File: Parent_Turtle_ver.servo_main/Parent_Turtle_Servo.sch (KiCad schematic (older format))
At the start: 42 parts, among them P1 CONN_02X15, P10 WRITING, P12 5V_in, P2 CONN_02X15, P3 CAN, P4 CAN, P5 PWM, P6 SERIAL0, P7 SERIAL1, P8 WRITING_IN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

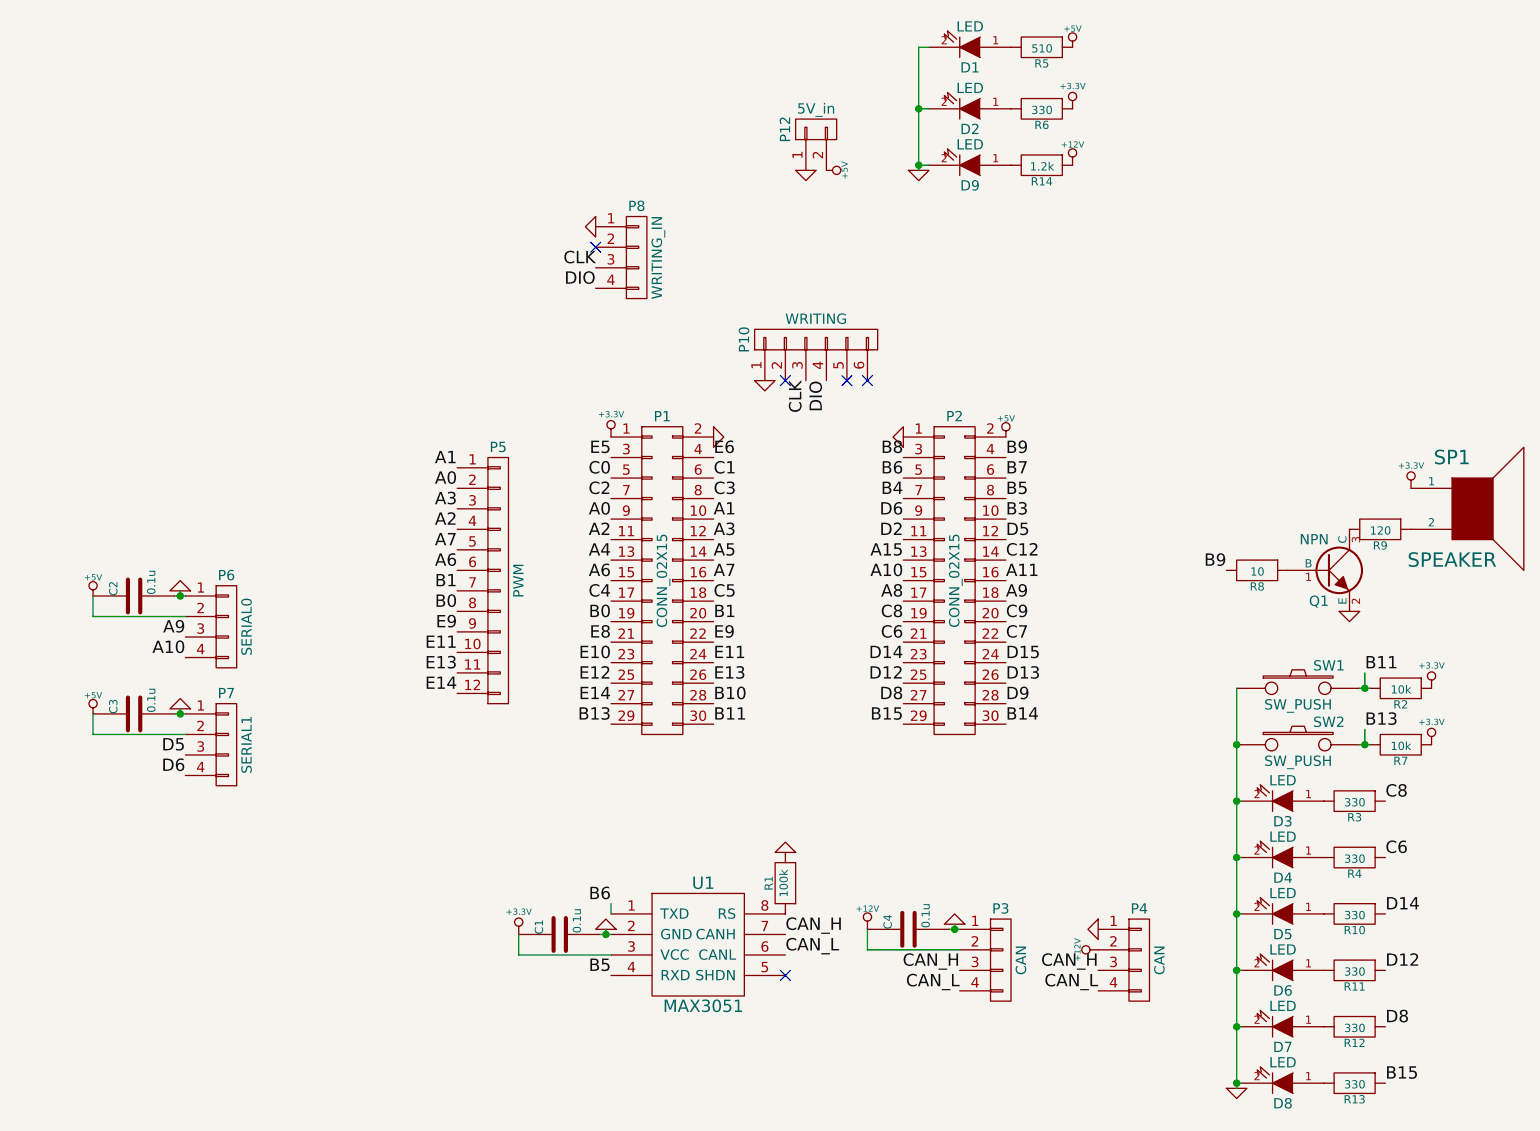
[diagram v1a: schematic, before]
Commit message: A/Dコンバータのピンの追加
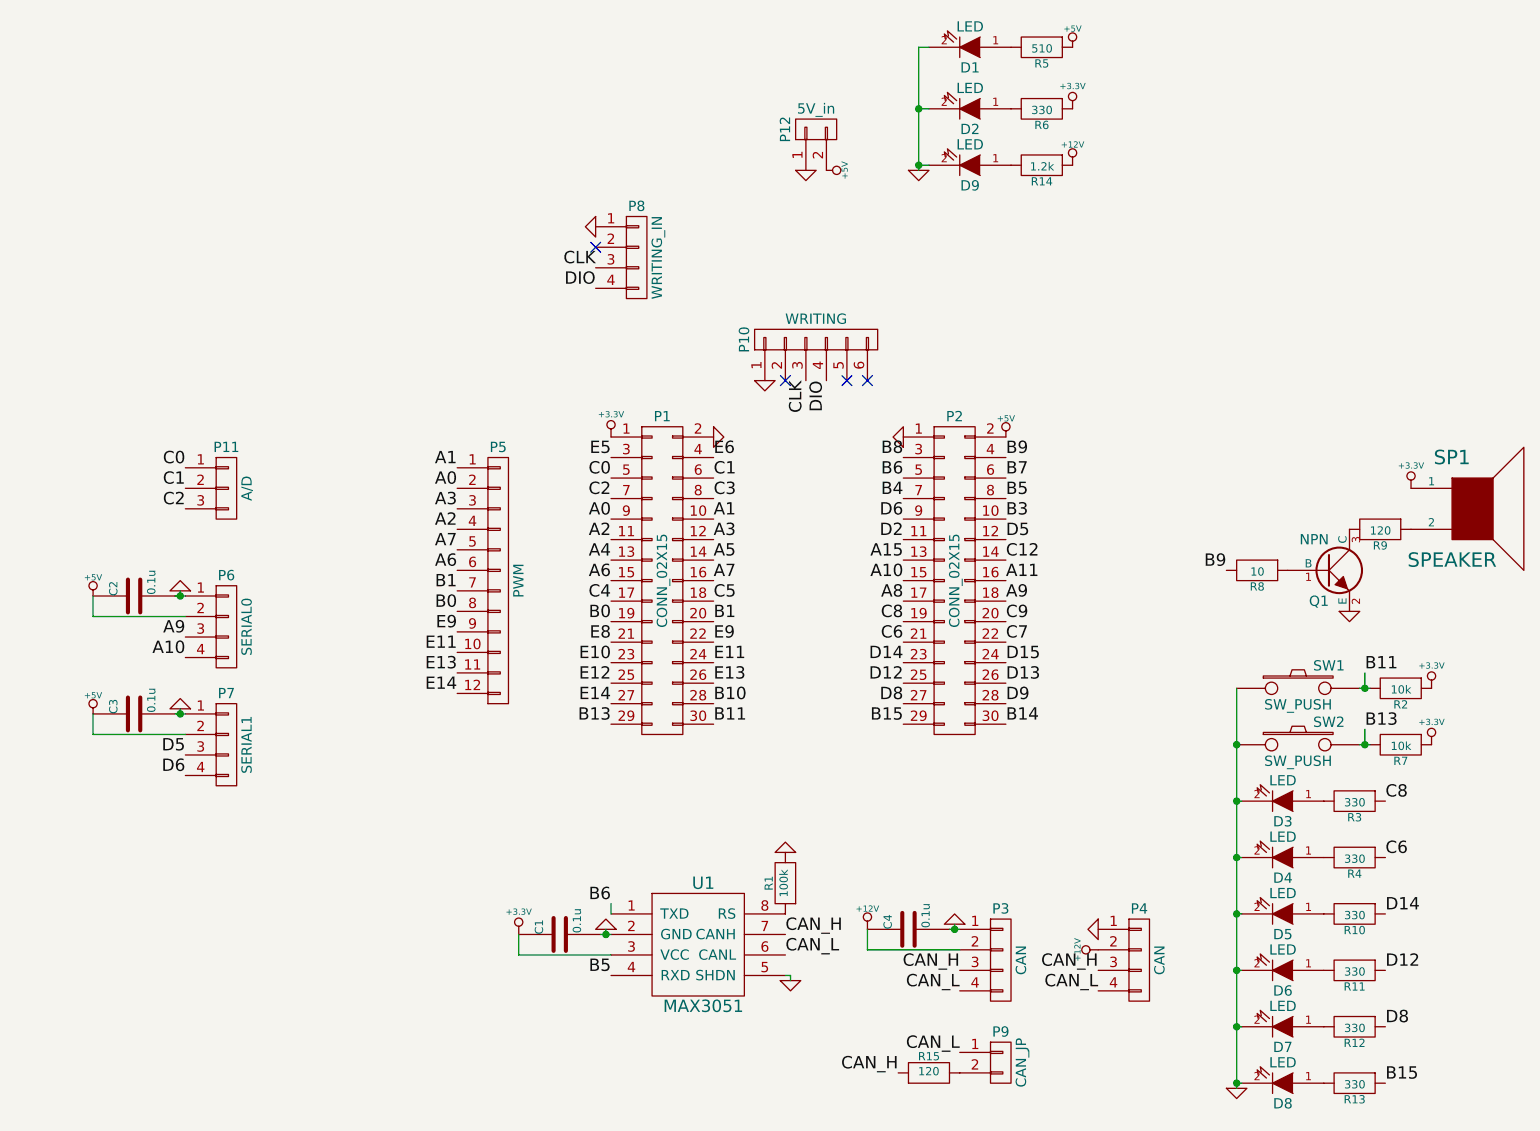
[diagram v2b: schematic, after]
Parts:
- added P11: A/D, Pin_Headers:Pin_Header_Straight_1x03, symbol CONN_01X03
- added P9: CAN_JP, Pin_Headers:Pin_Header_Straight_1x02, symbol CONN_01X02
- added R15: 120, Resistors_SMD:R_0603, symbol R
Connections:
- net C0: now also P11.1 (P1)
- net C1: now also P11.2 (P2)
- net C2: now also P11.3 (P3)
- net CAN_H: now also R15.1
- net CAN_L: now also P9.1 (P1)
- net GND: now also U1.5 (SHDN)
- new net: P9.2 (P2), R15.2
- no-connect marks 5 -> 4
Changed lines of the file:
@@
 LIBS:sample
 LIBS:ucc20520
-LIBS:Parent_Turtle_Enc-cache
+LIBS:Parent_Turtle_Servo-cache
 EELAYER 25 0
 EELAYER END
@@
 $EndComp
 $Comp
-L +5V #PWR18
+L +5V #PWR19
 U 1 1 5B3F2877
 P 7075 3150
-F 0 "#PWR18" H 7075 3240 20  0001 C CNN
+F 0 "#PWR19" H 7075 3240 20  0001 C CNN
 F 1 "+5V" H 7075 3240 30  0000 C CNN
 F 2 "" H 7075 3150 60  0000 C CNN
@@
 $EndComp
 $Comp
-L GND #PWR15
+L GND #PWR16
 U 1 1 5B3F2891
 P 6575 3150
-F 0 "#PWR15" H 6575 3150 30  0001 C CNN
+F 0 "#PWR16" H 6575 3150 30  0001 C CNN
 F 1 "GND" H 6575 3080 30  0001 C CNN
 F 2 "" H 6575 3150 60  0000 C CNN
@@
 $EndComp
 $Comp
-L GND #PWR12
+L GND #PWR13
 U 1 1 5B3F302D
 P 6100 1850
-F 0 "#PWR12" H 6100 1850 30  0001 C CNN
+F 0 "#PWR13" H 6100 1850 30  0001 C CNN
 F 1 "GND" H 6100 1780 30  0001 C CNN
 F 2 "" H 6100 1850 60  0000 C CNN
@@
 $EndComp
 $Comp
-L +5V #PWR13
+L +5V #PWR14
 U 1 1 5B3F3047
 P 6200 1850
-F 0 "#PWR13" H 6200 1940 20  0001 C CNN
+F 0 "#PWR14" H 6200 1940 20  0001 C CNN
 F 1 "+5V" H 6200 1940 30  0000 C CNN
 F 2 "" H 6200 1850 60  0000 C CNN
@@
 $EndComp
 $Comp
-L +5V #PWR19
+L +5V #PWR20
 U 1 1 5B3F3152
 P 7400 1250
-F 0 "#PWR19" H 7400 1340 20  0001 C CNN
+F 0 "#PWR20" H 7400 1340 20  0001 C CNN
 F 1 "+5V" H 7400 1340 30  0000 C CNN
 F 2 "" H 7400 1250 60  0000 C CNN
@@
 $EndComp
 $Comp
-L GND #PWR16
+L GND #PWR17
 U 1 1 5B3F3423
 P 6650 1850
-F 0 "#PWR16" H 6650 1850 30  0001 C CNN
+F 0 "#PWR17" H 6650 1850 30  0001 C CNN
 F 1 "GND" H 6650 1780 30  0001 C CNN
 F 2 "" H 6650 1850 60  0000 C CNN
@@
 $EndComp
 $Comp
-L +3.3V #PWR20
+L +3.3V #PWR21
 U 1 1 5B3F35B7
 P 7400 1550
-F 0 "#PWR20" H 7400 1510 30  0001 C CNN
+F 0 "#PWR21" H 7400 1510 30  0001 C CNN
 F 1 "+3.3V" H 7400 1660 30  0000 C CNN
 F 2 "" H 7400 1550 60  0000 C CNN
@@
 $EndComp
 $Comp
-L GND #PWR17
+L GND #PWR18
 U 1 1 5BC45FBD
 P 6825 5525
-F 0 "#PWR17" H 6825 5525 30  0001 C CNN
+F 0 "#PWR18" H 6825 5525 30  0001 C CNN
 F 1 "GND" H 6825 5455 30  0001 C CNN
 F 2 "" H 6825 5525 60  0000 C CNN
@@
 $EndComp
 $Comp
-L GND #PWR22
+L GND #PWR23
 U 1 1 5BC46188
 P 7525 5550
-F 0 "#PWR22" H 7525 5550 30  0001 C CNN
+F 0 "#PWR23" H 7525 5550 30  0001 C CNN
 F 1 "GND" H 7525 5480 30  0001 C CNN
 F 2 "" H 7525 5550 60  0000 C CNN
@@
 CAN_H
 $Comp
-L +12V #PWR23
+L +12V #PWR24
 U 1 1 5BC46309
 P 7525 5650
-F 0 "#PWR23" H 7525 5600 20  0001 C CNN
+F 0 "#PWR24" H 7525 5600 20  0001 C CNN
 F 1 "+12V" H 7525 5750 30  0000 C CNN
 F 2 "" H 7525 5650 60  0000 C CNN
@@
 $EndComp
 $Comp
-L +12V #PWR14
+L +12V #PWR15
 U 1 1 5BC46345
 P 6400 5550
-F 0 "#PWR14" H 6400 5500 20  0001 C CNN
+F 0 "#PWR15" H 6400 5500 20  0001 C CNN
 F 1 "+12V" H 6400 5650 30  0000 C CNN
 F 2 "" H 6400 5550 60  0000 C CNN
@@
 $EndComp
 $Comp
-L R R1
-U 1 1 5BC46B24
-P 6000 5325
-F 0 "R1" V 6080 5325 40  0000 C CNN
-F 1 "100k" V 6007 5326 40  0000 C CNN
-F 2 "Resistors_SMD:R_0603" V 5930 5325 30  0001 C CNN
-F 3 "" H 6000 5325 30  0000 C CNN
-	1    6000 5325
-	-1   0    0    1
-$EndComp
-$Comp
 L GND #PWR11
 U 1 1 5BC46BAA
@@
 Text Label 6000 5675 0    60   ~ 0
 CAN_L
-NoConn ~ 6000 5775
 $Comp
 L CONN_01X04 P7
@@
 $EndComp
 $Comp
-L GND #PWR24
+L GND #PWR25
 U 1 1 5BC4BE3D
 P 8200 6325
-F 0 "#PWR24" H 8200 6325 30  0001 C CNN
+F 0 "#PWR25" H 8200 6325 30  0001 C CNN
 F 1 "GND" H 8200 6255 30  0001 C CNN
 F 2 "" H 8200 6325 60  0000 C CNN
@@
 B9
 $Comp
-L GND #PWR25
+L GND #PWR26
 U 1 1 5BC4A745
 P 8750 4000
-F 0 "#PWR25" H 8750 4000 30  0001 C CNN
+F 0 "#PWR26" H 8750 4000 30  0001 C CNN
 F 1 "GND" H 8750 3930 30  0001 C CNN
 F 2 "" H 8750 4000 60  0000 C CNN
@@
 $EndComp
 $Comp
-L +3.3V #PWR26
+L +3.3V #PWR27
 U 1 1 5BC4AAE5
 P 9050 3400
-F 0 "#PWR26" H 9050 3360 30  0001 C CNN
+F 0 "#PWR27" H 9050 3360 30  0001 C CNN
 F 1 "+3.3V" H 9050 3510 30  0000 C CNN
 F 2 "" H 9050 3400 60  0000 C CNN
@@
 Connection ~ 8200 5200
 $Comp
-L +3.3V #PWR28
+L +3.3V #PWR29
 U 1 1 5BC4BBBA
 P 9150 4650
-F 0 "#PWR28" H 9150 4610 30  0001 C CNN
+F 0 "#PWR29" H 9150 4610 30  0001 C CNN
 F 1 "+3.3V" H 9150 4760 30  0000 C CNN
 F 2 "" H 9150 4650 60  0000 C CNN
@@
 $EndComp
 $Comp
-L +3.3V #PWR27
+L +3.3V #PWR28
 U 1 1 5BC4B59D
 P 9150 4375
-F 0 "#PWR27" H 9150 4335 30  0001 C CNN
+F 0 "#PWR28" H 9150 4335 30  0001 C CNN
 F 1 "+3.3V" H 9150 4485 30  0000 C CNN
 F 2 "" H 9150 4375 60  0000 C CNN
@@
 $EndComp
 $Comp
-L +12V #PWR21
+L +12V #PWR22
 U 1 1 5BC50D62
 P 7400 1825
-F 0 "#PWR21" H 7400 1775 20  0001 C CNN
+F 0 "#PWR22" H 7400 1775 20  0001 C CNN
 F 1 "+12V" H 7400 1925 30  0000 C CNN
 F 2 "" H 7400 1825 60  0000 C CNN
@@
 	1    0    0    -1
 $EndComp
+$Comp
+L CONN_01X02 P9
+U 1 1 5BC6ED99
+P 7050 6200
+F 0 "P9" H 7050 6350 50  0000 C CNN
+F 1 "CAN_JP" V 7150 6200 50  0000 C CNN
+F 2 "Pin_Headers:Pin_Header_Straight_1x02" H 7050 6200 50  0001 C CNN
+F 3 "" H 7050 6200 50  0000 C CNN
+	1    7050 6200
+	1    0    0    -1
+$EndComp
+Text Label 6850 6150 2    60   ~ 0
+CAN_L
+$Comp
+L R R15
+U 1 1 5BC6F197
+P 6700 6250
+F 0 "R15" V 6780 6250 40  0000 C CNN
+F 1 "120" V 6707 6251 40  0000 C CNN
+F 2 "Resistors_SMD:R_0603" V 6630 6250 30  0001 C CNN
+F 3 "" H 6700 6250 30  0000 C CNN
+	1    6700 6250
+	0    -1   -1   0
+$EndComp
+Text Label 6550 6250 2    60   ~ 0
+CAN_H
+$Comp
+L GND #PWR12
+U 1 1 5BD04D06
+P 6025 5800
+F 0 "#PWR12" H 6025 5800 30  0001 C CNN
+F 1 "GND" H 6025 5730 30  0001 C CNN
+F 2 "" H 6025 5800 60  0000 C CNN
+F 3 "" H 6025 5800 60  0000 C CNN
+	1    6025 5800
+	1    0    0    -1
+$EndComp
+Wire Wire Line
+	6025 5800 6025 5775
+Wire Wire Line
+	6025 5775 6000 5775
+$Comp
+L CONN_01X03 P11
+U 1 1 5BD05C31
+P 3275 3400
+F 0 "P11" H 3275 3600 50  0000 C CNN
+F 1 "A/D" V 3375 3400 50  0000 C CNN
+F 2 "Pin_Headers:Pin_Header_Straight_1x03" H 3275 3400 50  0001 C CNN
+F 3 "" H 3275 3400 50  0000 C CNN
+	1    3275 3400
+	1    0    0    -1
+$EndComp
+Text Label 3075 3300 2    60   ~ 0
+C0
+Text Label 3075 3400 2    60   ~ 0
+C1
+Text Label 3075 3500 2    60   ~ 0
+C2
+$Comp
+L R R1
+U 1 1 5BD073C8
+P 6000 5325
+F 0 "R1" V 6080 5325 40  0000 C CNN
+F 1 "100k" V 6007 5326 40  0000 C CNN
+F 2 "Resistors_SMD:R_0603" V 5930 5325 30  0001 C CNN
+F 3 "" H 6000 5325 30  0000 C CNN
+	1    6000 5325
+	-1   0    0    1
+$EndComp
 $EndSCHEMATC

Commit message: バージョンを上げた
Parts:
- removed P11: A/D, Pin_Headers:Pin_Header_Straight_1x03, symbol CONN_01X03
- added P11: A/D, Pin_Headers:Pin_Header_Straight_1x04, symbol CONN_01X04
- added P13: CONN_02X04, Pin_Headers:Pin_Header_Straight_2x04, symbol CONN_02X04
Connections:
- net +3.3V: now also P13.2 (P2), P13.4 (P4), P13.6 (P6), P13.8 (P8)
- net C0: now also P11.1 (P1)
- net C1: now also P11.2 (P2)
- net C2: now also P11.3 (P3)
- net C3: now also P11.4 (P4)
- net GND: now also P13.1 (P1), P13.3 (P3), P13.5 (P5), P13.7 (P7)
